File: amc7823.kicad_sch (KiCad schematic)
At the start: 9 parts, among them U1301 AMC7823IRTAT

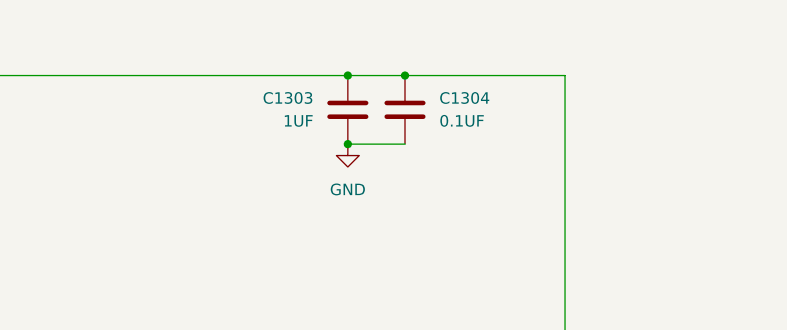
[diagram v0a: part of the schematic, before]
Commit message: Updates from Michal to fix ERC errors
Still lots of ERC warnings
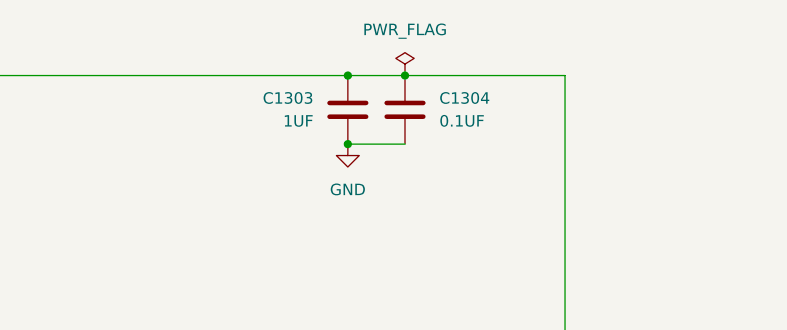
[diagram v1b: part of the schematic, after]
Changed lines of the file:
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@@
+	)
+	(symbol
+		(lib_id "power:PWR_FLAG")
+		(at 217.17 46.99 0)
+		(unit 1)
+		(exclude_from_sim no)
+		(in_bom yes)
+		(on_board yes)
+		(dnp no)
+		(fields_autoplaced yes)
+		(property "Reference" "#FLG011"
+			(at 217.17 45.085 0)
+			(effects
+				(font
+					(size 1.27 1.27)
+				)
+				(hide yes)
+			)
+		)
+		(property "Value" "PWR_FLAG"
+			(at 217.17 41.91 0)
+			(effects
+				(font
+					(size 1.27 1.27)
+				)
+			)
+		)
+		(property "Footprint" ""
+			(at 217.17 46.99 0)
+			(effects
+				(font
+					(size 1.27 1.27)
+				)
+				(hide yes)
+			)
+		)
+		(property "Datasheet" "~"
+			(at 217.17 46.99 0)
+			(effects
+				(font
+					(size 1.27 1.27)
+				)
+				(hide yes)
+			)
+		)
+		(property "Description" "Special symbol for telling ERC where power comes from"
+			(at 217.17 46.99 0)
+			(effects
+				(font
+					(size 1.27 1.27)
+				)
+				(hide yes)
+			)
+		)
+		(pin "1"
+		)
+		(instances
+			(project "zest"
+				(path "/00000000-0000-0000-0000-000000000003/00000000-0000-0000-0000-00000000000d"
+					(reference "#FLG011")
+					(unit 1)
+				)
+			)
+		)
 	)
 	(symbol

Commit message: Schematic Changes
Added Manufacturer/MPN/Description Fields to parts
Added libraries to project
Modified FMC schematic to use new symbol
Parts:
- C1301, C1304, C1305: Manufacturer (none) -> Murata; Manufacturer Part Number (none) -> GRM155R61A104KA01D
- C1302, C1303: Manufacturer (none) -> Murata; Manufacturer Part Number (none) -> GRM188R61E105KA12D
- R1301, R1302, R1303: Manufacturer (none) -> YAGEO; Manufacturer Part Number (none) -> RC0603FR-074K75L
- U1301: Manufacturer (none) -> Texas Instruments; Manufacturer Part Number (none) -> AMC7823IRTAT
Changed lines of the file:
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@@
 			)
 		)
-		(property "Description" "Unpolarized capacitor"
+		(property "Description" "CAP CER 0.1UF 10V X5R 0402"
 			(at 64.77 58.42 0)
 			(effects
@@
 		(property "Vendor" "digikey:490-1318-1-ND"
 			(at 0 0 0)
+			(effects
+				(font
+					(size 1.27 1.27)
+				)
+				(hide yes)
+			)
+		)
+		(property "Manufacturer" "Murata"
+			(at 64.77 58.42 0)
+			(effects
+				(font
+					(size 1.27 1.27)
+				)
+				(hide yes)
+			)
+		)
+		(property "Manufacturer Part Number" "GRM155R61A104KA01D"
+			(at 64.77 58.42 0)
 			(effects
 				(font
@@
 			)
 		)
-		(property "Description" "Unpolarized capacitor"
+		(property "Description" "CAP CER 1UF 25V X5R 0603"
 			(at 210.82 50.8 0)
 			(effects
@@
 		(property "Vendor" "digikey:490-3897-1-ND"
 			(at 421.64 101.6 0)
+			(effects
+				(font
+					(size 1.27 1.27)
+				)
+				(hide yes)
+			)
+		)
+		(property "Manufacturer" "Murata"
+			(at 210.82 50.8 0)
+			(effects
+				(font
+					(size 1.27 1.27)
+				)
+				(hide yes)
+			)
+		)
+		(property "Manufacturer Part Number" "GRM188R61E105KA12D"
+			(at 210.82 50.8 0)
 			(effects
 				(font
@@
 			)
 		)
-		(property "Description" "Resistor"
+		(property "Description" "RES 4.75K OHM 1% 1/10W 0603"
 			(at 214.63 120.65 0)
 			(effects
@@
 		(property "Vendor" "digikey:311-4.75KHRCT-ND"
 			(at 335.28 335.28 0)
+			(effects
+				(font
+					(size 1.27 1.27)
+				)
+				(hide yes)
+			)
+		)
+		(property "Manufacturer" "YAGEO "
+			(at 214.63 120.65 0)
+			(effects
+				(font
+					(size 1.27 1.27)
+				)
+				(hide yes)
+			)
+		)
+		(property "Manufacturer Part Number" "RC0603FR-074K75L "
+			(at 214.63 120.65 0)
 			(effects
 				(font
@@
 			)
 		)
-		(property "Description" "Unpolarized capacitor"
+		(property "Description" "CAP CER 1UF 25V X5R 0603"
 			(at 71.12 58.42 0)
 			(effects
@@
 		(property "Vendor" "digikey:490-3897-1-ND"
 			(at 0 116.84 0)
+			(effects
+				(font
+					(size 1.27 1.27)
+				)
+				(hide yes)
+			)
+		)
+		(property "Manufacturer" "Murata"
+			(at 71.12 58.42 0)
+			(effects
+				(font
+					(size 1.27 1.27)
+				)
+				(hide yes)
+			)
+		)
+		(property "Manufacturer Part Number" "GRM188R61E105KA12D"
+			(at 71.12 58.42 0)
 			(effects
 				(font
@@
 			)
 		)
-		(property "Description" ""
+		(property "Description" "IC ANLG MON/CTL 12B 200K 40WQFN"
 			(at 104.14 82.55 0)
 			(effects
@@
 		(property "Vendor" "digikey:296-18680-1-ND"
 			(at 0 165.1 0)
+			(effects
+				(font
+					(size 1.27 1.27)
+				)
+				(hide yes)
+			)
+		)
+		(property "Manufacturer" "Texas Instruments "
+			(at 104.14 82.55 0)
+			(effects
+				(font
+					(size 1.27 1.27)
+				)
+				(hide yes)
+			)
+		)
+		(property "Manufacturer Part Number" "AMC7823IRTAT "
+			(at 104.14 82.55 0)
 			(effects
 				(font
@@
 			)
 		)
-		(property "Description" "Resistor"
+		(property "Description" "RES 4.75K OHM 1% 1/10W 0603"
 			(at 73.66 87.63 0)
 			(effects
@@
 		(property "Vendor" "digikey:311-4.75KHRCT-ND"
 			(at 161.29 161.29 0)
+			(effects
+				(font
+					(size 1.27 1.27)
+				)
+				(hide yes)
+			)
+		)
+		(property "Manufacturer" "YAGEO "
+			(at 73.66 87.63 0)
+			(effects
+				(font
+					(size 1.27 1.27)
+				)
+				(hide yes)
+			)
+		)
+		(property "Manufacturer Part Number" "RC0603FR-074K75L "
+			(at 73.66 87.63 0)
 			(effects
 				(font
@@
 			)
 		)
-		(property "Description" "Unpolarized capacitor"
+		(property "Description" "CAP CER 0.1UF 10V X5R 0402"
 			(at 217.17 138.43 0)
 			(effects
@@
 		(property "Vendor" "digikey:490-1318-1-ND"
 			(at 434.34 0 0)
+			(effects
+				(font
+					(size 1.27 1.27)
+				)
+				(hide yes)
+			)
+		)
+		(property "Manufacturer" "Murata"
+			(at 217.17 138.43 0)
+			(effects
+				(font
+					(size 1.27 1.27)
+				)
+				(hide yes)
+			)
+		)
+		(property "Manufacturer Part Number" "GRM155R61A104KA01D"
+			(at 217.17 138.43 0)
 			(effects
 				(font
@@
 			)
 		)
-		(property "Description" "Unpolarized capacitor"
+		(property "Description" "CAP CER 0.1UF 10V X5R 0402"
 			(at 217.17 50.8 0)
 			(effects
@@
 			)
 		)
+		(property "Manufacturer" "Murata"
+			(at 217.17 50.8 0)
+			(effects
+				(font
+					(size 1.27 1.27)
+				)
+				(hide yes)
+			)
+		)
+		(property "Manufacturer Part Number" "GRM155R61A104KA01D"
+			(at 217.17 50.8 0)
+			(effects
+				(font
+					(size 1.27 1.27)
+				)
+				(hide yes)
+			)
+		)
 		(pin "2"
 		)
@@
 			)
 		)
-		(property "Description" "Resistor"
+		(property "Description" "RES 4.75K OHM 1% 1/10W 0603"
 			(at 100.33 90.17 0)
 			(effects
@@
 			(effects
 				(font
+					(size 1.27 1.27)
+				)
+				(hide yes)
+			)
+		)
+		(property "Manufacturer" "YAGEO "
+			(at 100.33 90.17 0)
+			(effects
+				(font
+					(size 1.27 1.27)
+				)
+				(hide yes)
+			)
+		)
+		(property "Manufacturer Part Number" "RC0603FR-074K75L "
+			(at 100.33 90.17 0)
+			(effects
+				(font

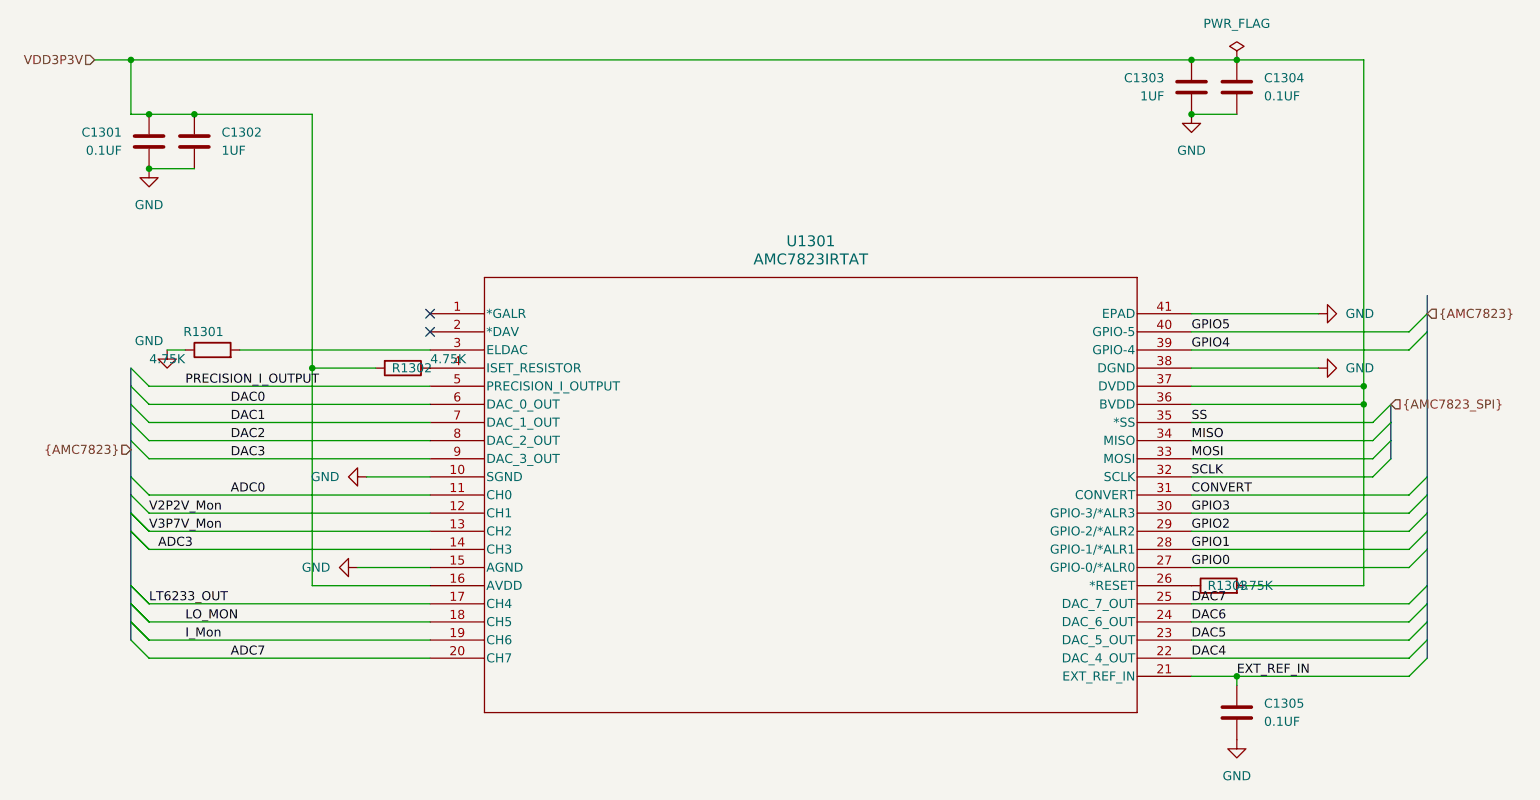
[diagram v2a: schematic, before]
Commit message: Schematics update
Cleaned up RF ADC and front end sections.
Verified that changes did not changes anything about the layout.
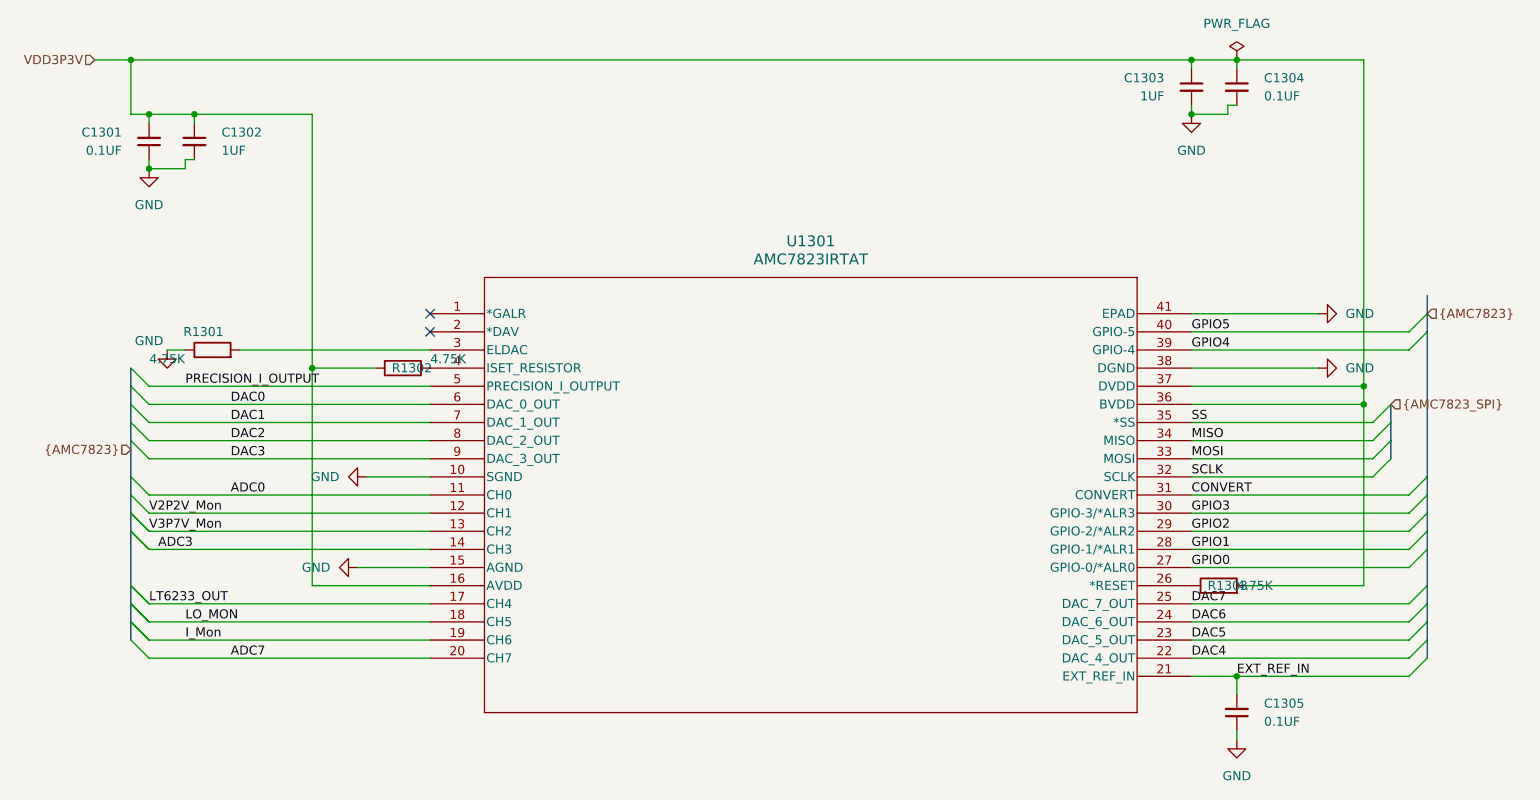
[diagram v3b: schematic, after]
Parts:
- C1301, C1302, C1303, C1304, C1305: symbol Device:C -> Device:C_Small
